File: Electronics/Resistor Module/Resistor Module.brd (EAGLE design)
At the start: 50 x 50 mm, 59 parts, among them IC1 74HC595D, IC2 74HC595D, U1 25AA010A

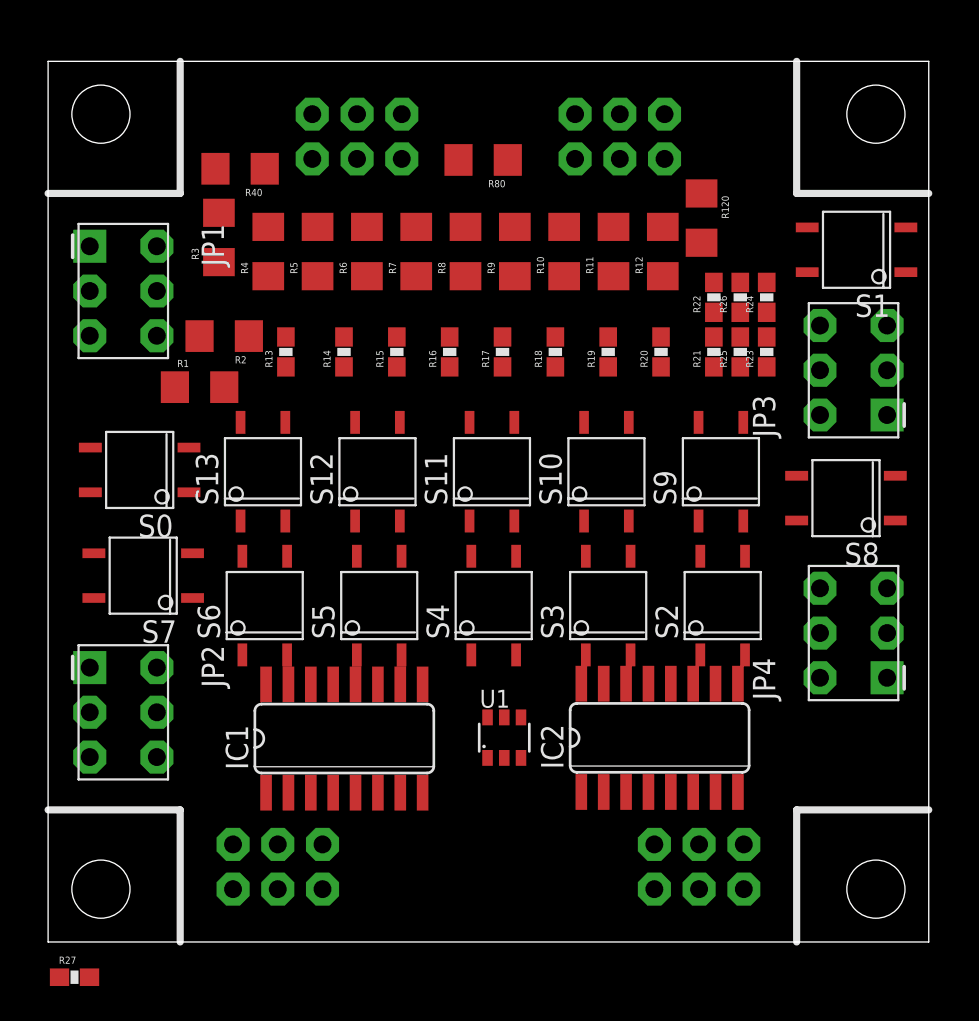
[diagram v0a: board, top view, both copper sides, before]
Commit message: Finished layout of resistor module
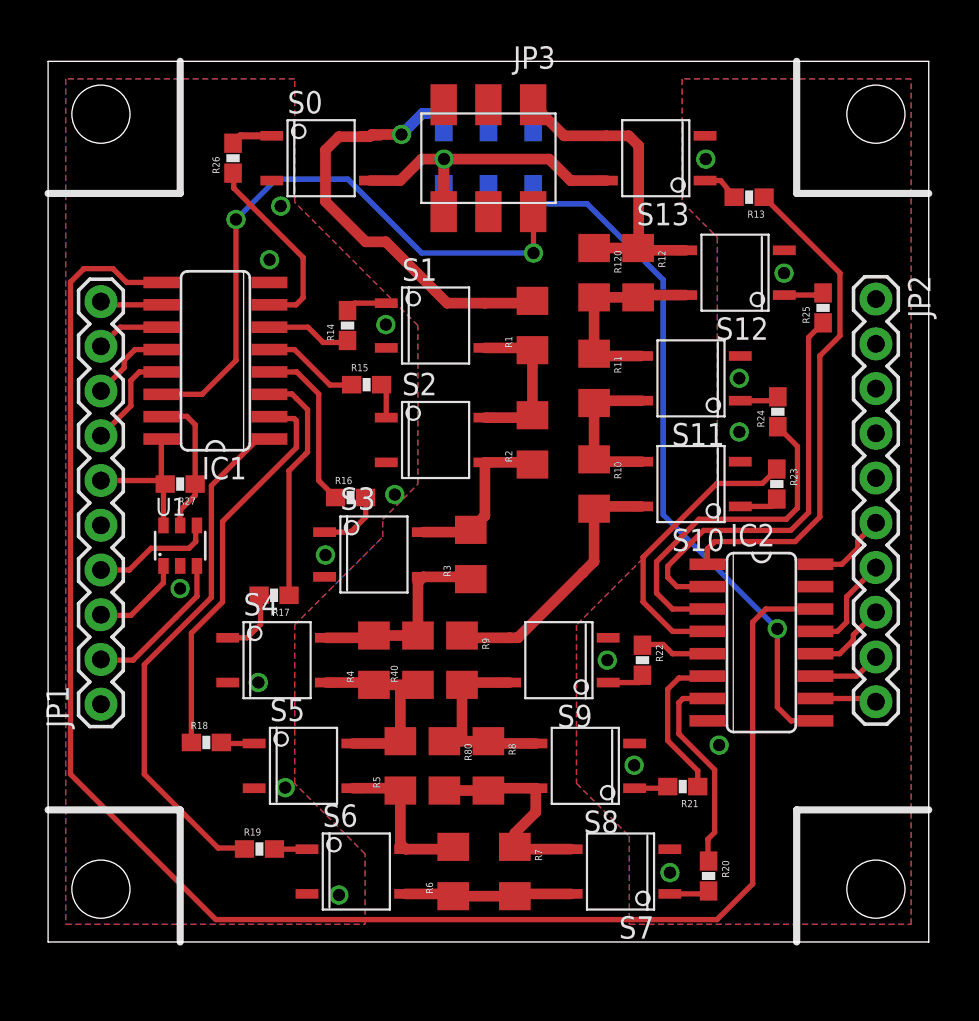
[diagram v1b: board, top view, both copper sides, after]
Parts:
- removed JP5, JP6, JP7, JP8: (no value), Resistor Module Library:4-103240-0-03
- JP1, JP2: value (none) -> M10PASSTHROUGH; device Resistor Module Library:535542-3 -> Resistor Module Library:U4CON_18688_10
- JP3: device Resistor Module Library:535542-3 -> Resistor Module Library:969973-3
- JP4: device Resistor Module Library:535542-3 -> Resistor Module Library:2X3_SMT-M0.1
- moved JP2 48.7 mm to (47.0, 36.5)
- moved JP4 36.8 mm to (25.0, 44.5), flipped to the bottom, turned to 180 degrees
- moved R7 35.6 mm to (26.5, 4.00), turned to 270 degrees
- moved R6 35.5 mm to (23.0, 4.00)
- moved R19 34.5 mm to (12.0, 5.28), turned to 0 degrees
- moved R80 34.5 mm to (22.5, 10.0), turned to 270 degrees
- moved S7 31.9 mm to (32.5, 4.00)
- moved R20 29.9 mm to (37.5, 3.75), turned to 270 degrees
- moved R26 29.9 mm to (10.5, 44.5)
- moved R18 29.7 mm to (8.98, 11.3), turned to 0 degrees
- moved R40 29.7 mm to (21.0, 16.0), turned to 90 degrees
- moved R5 29.6 mm to (20.0, 10.0)
- moved R8 29.2 mm to (25.0, 10.0), turned to 270 degrees
- moved R27 28.6 mm to (7.50, 26.0), turned to 180 degrees
- moved S13 28.5 mm to (34.5, 44.5), turned to 90 degrees
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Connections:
- net N$1 renamed SERIAL_PASS
- removed net N$20 (its old number): IC1.6, R19.1
- removed net N$27: IC2.4, R25.1
- removed net N$28: IC2.5, R26.1
- new net 5V_2: IC2.16, JP2.6
- new net GND_2: IC2.8, JP2.5, S10.P2, S11.P2, S12.P2, S13.P2, S7.P2, S8.P2, S9.P2
- new net N$1: IC1.7, R26.1
- new net N$13: IC1.4, R16.1
- new net N$14: IC1.3, R17.1
- new net SERIAL_CLK_2: IC2.11, JP2.9
- new net SERIAL_LATCH_2: IC2.12, JP2.8
- new net SERIAL_MR_L_2: IC2.10, JP2.10
- new net SERIAL_OE_L_2: IC2.13, JP2.7
- net 5V: now also JP1.6; no longer IC2.16, JP4.1, JP8.5
- net EEPROM_CS_L: now also IC1.15; no longer IC2.6
- net EEPROM_MISO: now also JP1.4; no longer JP4.4, JP8.4
- net EEPROM_MOSI: now also JP1.2; no longer JP4.2, JP8.6
- net EEPROM_SCK: now also JP1.3; no longer JP4.6, JP8.2
- net GND: now also JP1.5; no longer IC2.8, JP4.5, JP8.1, S10.P2, S11.P2, S12.P2, S13.P2, S7.P2, S8.P2, S9.P2
- net N$12: now also IC1.5, R15.1; no longer IC1.1, R14.1
- net N$16: now also R18.1; no longer R15.1
- net N$17: now also IC1.1, R19.1; no longer IC1.3, R16.1
- net N$18: now also IC2.1, R13.1; no longer IC1.4, R17.1
- net N$19: now also IC2.2, R25.1; no longer IC1.5, R18.1
- net N$2: now also IC1.6, R14.1; no longer IC1.15, R13.1
- net N$21: now also IC2.4, R23.1; no longer IC1.7, R20.1
- net N$22: now also IC2.5, R22.1; no longer IC2.15, R21.1
- net N$23: now also IC2.6, R21.1; no longer IC2.1, R22.1
- net N$24: now also IC2.7, R20.1; no longer IC2.2, R23.1
- net RELAY_POST_SHORT: now also S0.P1; no longer S13.P1
- net RELAY_PRE_SHORT: now also S13.P1; no longer S0.P1
- net R_DOWNSTREAM_IN: now also JP3.1, R12.1, R120.1, S12.P3, S13.P3; no longer JP3.5, JP3.6, R1.2, S0.P4, S1.P4
- net R_DOWNSTREAM_OUT: now also JP4.1, R1.2, S0.P4, S1.P4; no longer JP7.1, JP7.2, R12.1, R120.1, S12.P3, S13.P3
- net R_UPSTREAM: now also JP3.6, JP4.2; no longer JP3.1, JP3.2, JP7.5, JP7.6
- net SERIAL_CLK: now also JP1.9; no longer IC2.11, JP2.3, JP6.3
- net SERIAL_IN: now also JP3.2; no longer JP2.1
- net SERIAL_LATCH: now also JP1.8; no longer IC2.12, JP2.5, JP6.1
- net SERIAL_MR_L: now also JP1.10; no longer IC2.10, JP2.6, JP6.2
- net SERIAL_OE_L: now also JP1.7; no longer IC2.13, JP2.4, JP6.4
- net SERIAL_OUT: now also JP4.6; no longer JP6.5
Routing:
- net SERIAL_PASS: track 0.00 -> 95.5 mm
- net SERIAL_OUT: track 0.00 -> 38.6 mm, vias 0 -> 1
- net SERIAL_IN: track 0.00 -> 35.0 mm, vias 0 -> 2
- net N$17: track 0.00 -> 29.8 mm
- net N$18: track 0.00 -> 28.4 mm
- net R_DOWNSTREAM_OUT: track 0.00 -> 24.7 mm, vias 0 -> 1
- net N$19: track 0.00 -> 23.5 mm
- net N$16: track 0.00 -> 22.4 mm
- net R_UPSTREAM: track 0.00 -> 19.9 mm, vias 0 -> 1
- net N$20: track 0.00 -> 19.4 mm
- net R_DOWNSTREAM_IN: track 0.00 -> 18.0 mm
- net N$21: track 0.00 -> 16.5 mm
- net N$10: track 0.00 -> 15.1 mm
- net N$14: track 0.00 -> 13.5 mm
- net N$8: track 0.00 -> 12.3 mm
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- added copper zone on layer 1, net GND
- added copper zone on layer 16, net GND
- added copper zone on layer 1, net GND_2
- added copper zone on layer 16, net GND_2

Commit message: Finished layout and updated sketch. Discovered I could fit entire range on a single node if I double back the thing, so gonna do that instead. Who needs modularity when the entire thing fits on one board?
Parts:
- added C1, C2, C3: 1uF, Resistor Module Library:0603-CAP
- moved R27 1.80 mm to (7.25, 24.2)
- moved U1 1.57 mm to (7.88, 21.0)
- moved R17 0.38 mm to (13.2, 19.7)
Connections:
- net 5V: now also C1.1, C3.2
- net 5V_2: now also C2.1
- net GND: now also C1.2, C3.1
- net GND_2: now also C2.2
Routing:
- net GND: track 0.00 -> 7.35 mm
- net 5V: track 8.77 -> 13.8 mm
- net 5V_2: track 4.65 -> 7.31 mm
- net EEPROM_MISO: track 7.00 -> 9.20 mm, vias 0 -> 1
- net EEPROM_CS_L: track 8.21 -> 9.55 mm
- net EEPROM_MOSI: track 8.69 -> 7.77 mm
- net EEPROM_SCK: track 5.29 -> 4.49 mm

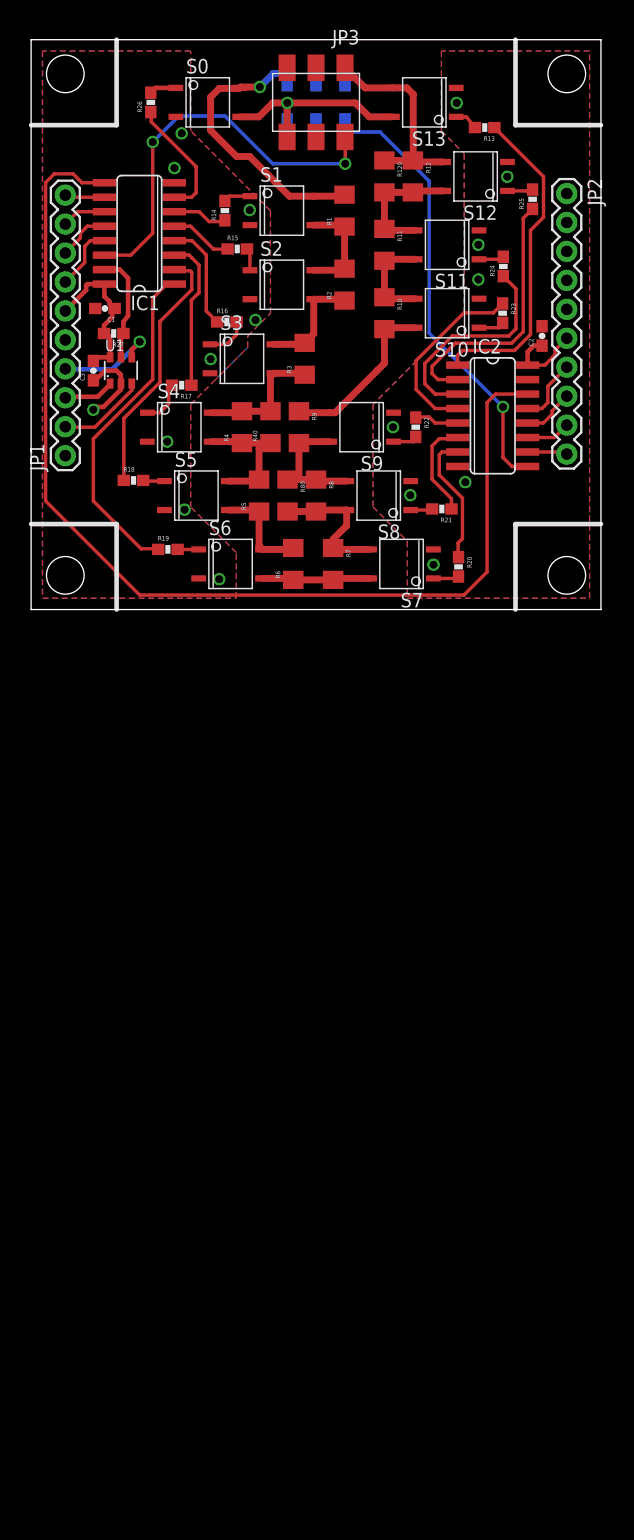
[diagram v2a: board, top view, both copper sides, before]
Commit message: Reworking resistor module to fit everything on a single module
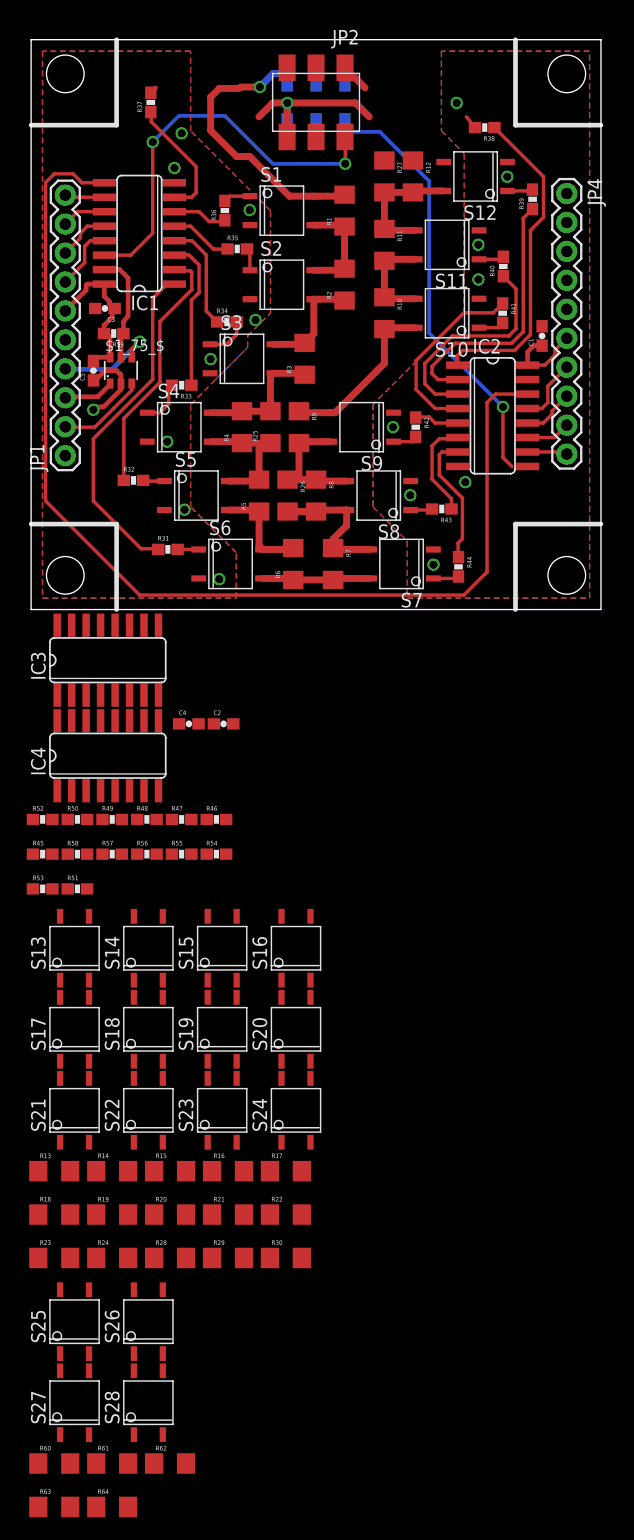
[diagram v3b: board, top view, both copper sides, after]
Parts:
- removed R120: 1k, Resistor Module Library:1206
- removed R80: 100, Resistor Module Library:1206
- removed S0: CPC1002N, Resistor Module Library:CPC1002N
- added C4, C5: 1uF, Resistor Module Library:0603-CAP
- added IC3, IC4: 74HC595D, Resistor Module Library:SO16
- added R28: 10k, Resistor Module Library:1206
- added R29: 100k, Resistor Module Library:1206
- added R30, R60: 1M, Resistor Module Library:1206
- added R31, R32, R33, R34, R35, R36, R37, R38, R39, R41, R42, R43, R44, R45, R46, R47, R48, R49, R50, R51, R52, R53, R54, R55, R56, R57, R58: 2k, Resistor Module Library:0603-RES
- added R59: 10k, Resistor Module Library:0603-RES
- added R61, R62: 2M, Resistor Module Library:1206
- added R63, R64: 10M, Resistor Module Library:1206
- added S14, S15, S16, S17, S18, S19, S20, S21, S22, S23, S24, S25, S26, S27, S28: CPC1002N, Resistor Module Library:CPC1002N
- JP2: value M10PASSTHROUGH -> (none); device Resistor Module Library:U4CON_18688_10 -> Resistor Module Library:969973-3
- JP3: device Resistor Module Library:969973-3 -> Resistor Module Library:2X3_SMT-M0.1
- JP4: value (none) -> M10PASSTHROUGH; device Resistor Module Library:2X3_SMT-M0.1 -> Resistor Module Library:U4CON_18688_10
- R13: value 2k -> 1k; device Resistor Module Library:0603-RES -> Resistor Module Library:1206
- R14, R15: device Resistor Module Library:0603-RES -> Resistor Module Library:1206
- R16, R17: value 2k -> 10k; device Resistor Module Library:0603-RES -> Resistor Module Library:1206
- R18, R19: value 2k -> 20k; device Resistor Module Library:0603-RES -> Resistor Module Library:1206
- R20, R21: value 2k -> 100k; device Resistor Module Library:0603-RES -> Resistor Module Library:1206
- R22, R23: value 2k -> 200k; device Resistor Module Library:0603-RES -> Resistor Module Library:1206
- R24: value 2k -> 1M; device Resistor Module Library:0603-RES -> Resistor Module Library:1206
- R25: value 2k -> 10; device Resistor Module Library:0603-RES -> Resistor Module Library:1206
- R26: value 2k -> 100; device Resistor Module Library:0603-RES -> Resistor Module Library:1206
- R27: value 10k -> 1k; device Resistor Module Library:0603-RES -> Resistor Module Library:1206
- R40: value 10 -> 2k; device Resistor Module Library:1206 -> Resistor Module Library:0603-RES
- moved R13 99.0 mm to (2.03, -49.3), turned to 0 degrees
- moved R24 93.5 mm to (7.11, -56.9), turned to 0 degrees
- moved R23 91.8 mm to (2.03, -56.9), turned to 0 degrees
- moved R14 84.9 mm to (7.11, -49.3), turned to 0 degrees
- moved R15 81.1 mm to (12.2, -49.3)
- moved S13 80.3 mm to (3.81, -29.7), turned to 0 degrees
- moved R16 74.5 mm to (17.3, -49.3)
- moved R22 70.0 mm to (22.4, -53.1), turned to 0 degrees
- moved R17 69.6 mm to (22.4, -49.3), turned to 0 degrees
- moved R18 64.8 mm to (2.03, -53.1)
- moved R21 64.7 mm to (17.3, -53.1), turned to 0 degrees
- moved R20 62.2 mm to (12.2, -53.1), turned to 0 degrees
- moved R19 58.6 mm to (7.11, -53.1)
- moved C2 44.0 mm to (16.9, -10.0), turned to 0 degrees
- moved C1 38.4 mm to (44.8, 24.0), turned to 90 degrees
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- renumbered U1 to $1_75_$
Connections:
- new net N$26: IC3.7, R51.1
- new net N$27: IC3.6, R50.1
- new net N$28: IC3.5, R49.1
- new net N$29: IC3.4, R48.1
- new net N$30: IC3.3, R47.1
- new net N$31: IC3.2, R46.1
- new net N$32: IC3.1, R45.1
- new net N$33: IC4.1, R52.1
- new net N$34: IC4.2, R53.1
- new net N$35: IC4.3, R54.1
- new net N$36: IC4.4, R55.1
- new net N$37: IC4.5, R56.1
- new net N$38: IC4.6, R57.1
- new net N$39: IC4.7, R58.1
- new net N$40: R12.1, R13.2, R27.1, S12.P3, S13.P4
- new net N$41: R14.1, R15.2, S14.P3, S15.P4
- new net N$42: R15.1, R16.2, R28.2, S15.P3, S16.P4
- new net N$43: R16.1, R17.2, R28.1, S16.P3, S17.P4
- new net N$44: R17.1, R18.2, S17.P3, S18.P4
- new net N$45: R18.1, R19.2, S18.P3, S19.P4
- new net N$46: R19.1, R20.2, R29.2, S19.P3, S20.P4
- new net N$47: R20.1, R21.2, R29.1, S20.P3, S21.P4
- new net N$48: R21.1, R22.2, S21.P3, S22.P4
- new net N$49: R22.1, R23.2, S22.P3, S23.P4
- new net N$50: R23.1, R24.2, R30.2, S23.P3, S24.P4
- new net N$51: R13.1, R14.2, S13.P3, S14.P4
- new net N$52: R24.1, R30.1, R60.2, S24.P3, S25.P4
- new net N$54: R60.1, R61.2, S25.P3, S26.P4
- new net N$55: R61.1, R62.2, S26.P3, S27.P4
- new net N$56: R62.1, R63.2, R64.2, S27.P3, S28.P4
- new net N$57: R63.1, R64.1, S28.P3
- new net RELAY_R13: S13.P1
- new net RELAY_R14: S14.P1
- new net RELAY_R15: S15.P1
- new net RELAY_R16: S16.P1
- new net RELAY_R17: S17.P1
- new net RELAY_R18: S18.P1
- new net RELAY_R19: S19.P1
- new net RELAY_R20: S20.P1
- new net RELAY_R21: S21.P1
- new net RELAY_R22: S22.P1
- new net RELAY_R23: S23.P1
- new net RELAY_R24: S24.P1
- new net RELAY_R25: S25.P1
- new net RELAY_R26: S26.P1
- new net RELAY_R27: S27.P1
- new net RELAY_R28: S28.P1
- new net R_IN: R1.2, S1.P4
- new net SERIAL_PASS1: IC2.9, IC3.14
- new net SERIAL_PASS2: IC3.9, IC4.14
- net 5V: now also C3.1, C4.1, C5.2, IC3.16, R59.2; no longer C1.1, C3.2, R27.2
- net 5V_2: now also C1.1, IC4.16, JP4.6; no longer JP2.6
- net EEPROM_CS_L: now also IC3.15, R59.1; no longer R27.1
- net GND: now also C3.2, C4.2, C5.1, IC3.8, S10.P2, S11.P2, S12.P2, S13.P2, S14.P2, S15.P2, S16.P2, S17.P2, S18.P2, S19.P2, S20.P2, S21.P2, S22.P2, S23.P2, S24.P2, S25.P2, S26.P2, S27.P2, S28.P2, S7.P2, S8.P2, S9.P2; no longer C1.2, C3.1, S0.P2
- net GND_2: now also C1.2, IC4.8, JP4.5; no longer JP2.5, S10.P2, S11.P2, S12.P2, S13.P2, S7.P2, S8.P2, S9.P2
- net N$1: now also R37.1; no longer R26.1
- net N$12: now also R35.1; no longer R15.1
- net N$13: now also R34.1; no longer R16.1
- net N$14: now also R33.1; no longer R17.1
- net N$15: now also R27.2; no longer R120.2
- net N$16: now also R32.1; no longer R18.1
- net N$17: now also R31.1; no longer R19.1
- net N$18: now also R38.1; no longer R13.1
- net N$19: now also R39.1; no longer R25.1
- net N$2: now also R36.1; no longer R14.1
- net N$20: now also R40.1; no longer R24.1
- net N$21: now also R41.1; no longer R23.1
- net N$22: now also R42.1; no longer R22.1
- net N$23: now also R43.1; no longer R21.1
- net N$24: now also R44.1; no longer R20.1
- net N$4: now also R25.2; no longer R40.2
- net N$5: now also R25.1; no longer R40.1
- net N$8: now also R26.2; no longer R80.2
- net N$9: now also R26.1; no longer R80.1
- net RELAY_POST_SHORT: now also R37.2, R51.2; no longer R26.2, S0.P1
- net RELAY_PRE_SHORT: now also R38.2, R52.2; no longer R13.2, S13.P1
- net RELAY_R1: now also R36.2, R50.2; no longer R14.2
- net RELAY_R10: now also R41.2, R55.2; no longer R23.2
- net RELAY_R11: now also R40.2, R54.2; no longer R24.2
- net RELAY_R12: now also R39.2, R53.2; no longer R25.2
- net RELAY_R2: now also R35.2, R49.2; no longer R15.2
- net RELAY_R3: now also R34.2, R48.2; no longer R16.2
- net RELAY_R4: now also R33.2, R47.2; no longer R17.2
- net RELAY_R5: now also R32.2, R46.2; no longer R18.2
- net RELAY_R6: now also R31.2, R45.2; no longer R19.2
- net RELAY_R7: now also R44.2, R58.2; no longer R20.2
- net RELAY_R8: now also R43.2, R57.2; no longer R21.2
- net RELAY_R9: now also R42.2, R56.2; no longer R22.2
- net R_DOWNSTREAM_IN: now also JP2.1; no longer JP3.1, R12.1, R120.1, S12.P3, S13.P3
- net R_DOWNSTREAM_OUT: now also JP3.1; no longer JP4.1, R1.2, S0.P4, S1.P4
- net R_UPSTREAM: now also JP2.6, JP3.2; no longer JP3.6, JP4.2, S0.P3, S13.P4
- net SERIAL_CLK: now also IC3.11
- net SERIAL_CLK_2: now also IC4.11, JP4.9; no longer JP2.9
- net SERIAL_IN: now also JP2.2; no longer JP3.2
- net SERIAL_LATCH: now also IC3.12
- net SERIAL_LATCH_2: now also IC4.12, JP4.8; no longer JP2.8
- net SERIAL_MR_L: now also IC3.10
- net SERIAL_MR_L_2: now also IC4.10, JP4.10; no longer JP2.10
- net SERIAL_OE_L: now also IC3.13
- net SERIAL_OE_L_2: now also IC4.13, JP4.7; no longer JP2.7
- net SERIAL_OUT: now also JP3.6; no longer IC2.9, JP4.6
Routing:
- net R_DOWNSTREAM_OUT: track 24.7 -> 4.58 mm
- net R_IN: track 0.00 -> 19.9 mm
- net R_DOWNSTREAM_IN: track 18.0 -> 2.50 mm
- net R_UPSTREAM: track 19.9 -> 16.2 mm
- net RELAY_POST_SHORT: track 2.37 -> 0.59 mm
- net SERIAL_OUT: track 38.6 -> 37.2 mm
- net RELAY_PRE_SHORT: track 2.10 -> 1.21 mm
